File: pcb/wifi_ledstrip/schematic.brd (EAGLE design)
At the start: 80 x 49.5 mm, 64 parts, among them IC1 STM32F10XCXT6, Q1 8MHz

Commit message: gerber files exported
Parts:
- moved C1 0.61 mm to (69.4, 34.9)
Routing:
- net GND: track 350.7 -> 351.5 mm
- removed copper zone on layer 16, net SIGNATURE
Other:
- board text added: "v1.0"
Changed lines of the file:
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@@
 <text x="15.42" y="8.91" size="1.778" layer="21">+12V</text>
 <text x="42.672" y="9.144" size="1.778" layer="21">+12V</text>
-<text x="28.448" y="44.5008" size="1.778" layer="16" rot="MR0">Made by</text>
-<text x="28.448" y="41.2496" size="1.778" layer="16" rot="MR0">Daniel Tar</text>
-<text x="28.448" y="37.9984" size="1.778" layer="16" rot="MR0">30.07.2018</text>
+<text x="28.448" y="44.5008" size="1.778" layer="26" rot="MR0">Made by</text>
+<text x="28.448" y="41.2496" size="1.778" layer="26" rot="MR0">Daniel Tar</text>
+<text x="28.448" y="37.9984" size="1.778" layer="26" rot="MR0">30.07.2018</text>
+<text x="28.448" y="35.3568" size="1.778" layer="26" rot="MR0">v1.0</text>
 </plain>
 <attributes>
@@
 <attribute name="VALUE" x="66.17" y="38.81" size="1.27" layer="27" rot="R90"/>
 </element>
-<element name="C1" library="rcl" library_urn="urn:adsk.eagle:library:334" package="C1206" package3d_urn="urn:adsk.eagle:package:23618/2" value="" x="68.79" y="34.92" rot="R270">
-<attribute name="SPICEPREFIX" value="C" x="68.79" y="34.92" size="1.778" layer="27" rot="R270" display="off"/>
+<element name="C1" library="rcl" library_urn="urn:adsk.eagle:library:334" package="C1206" package3d_urn="urn:adsk.eagle:package:23618/2" value="" x="69.3996" y="34.92" rot="R270">
+<attribute name="SPICEPREFIX" value="C" x="69.3996" y="34.92" size="1.778" layer="27" rot="R270" display="off"/>
 </element>
 <element name="R7" library="rcl" library_urn="urn:adsk.eagle:library:334" package="R1206" package3d_urn="urn:adsk.eagle:package:23540/2" value="" x="23.42" y="47.29" rot="R180">
@@
 <wire x1="76.17" y1="21.17" x2="76.13" y2="21.21" width="0.2032" layer="1"/>
 <wire x1="77.75" y1="22.83" x2="76.13" y2="21.21" width="0.2032" layer="1"/>
-<wire x1="68.79" y1="33.52" x2="68.3775" y2="33.1075" width="0.508" layer="1"/>
-<wire x1="68.3775" y1="33.1075" x2="66.165" y2="33.1075" width="0.508" layer="1"/>
+<wire x1="69.3996" y1="33.52" x2="68.9871" y2="33.1075" width="0.508" layer="1"/>
+<wire x1="68.9871" y1="33.1075" x2="66.165" y2="33.1075" width="0.508" layer="1"/>
 <wire x1="76.16" y1="10.97" x2="76.16" y2="9.27" width="0.508" layer="1"/>
 <wire x1="76.16" y1="9.27" x2="73.25" y2="6.36" width="0.508" layer="1"/>
@@
 <wire x1="76.33" y1="46.17" x2="77.75" y2="44.75" width="0.508" layer="1"/>
 <wire x1="73.33" y1="46.17" x2="76.33" y2="46.17" width="0.508" layer="1"/>
-<wire x1="68.79" y1="33.52" x2="68.75" y2="33.48" width="0.5588" layer="1"/>
+<wire x1="69.3996" y1="33.52" x2="68.75" y2="32.8704" width="0.5588" layer="1"/>
 <via x="68.75" y="31.75" extent="1-16" drill="0.35"/>
 <wire x1="68.75" y1="31.75" x2="68.75" y2="23" width="0.5588" layer="16"/>
 <wire x1="65" y1="19.25" x2="64.75" y2="19.25" width="0.5588" layer="16"/>
 <via x="64.75" y="19.25" extent="1-16" drill="0.35"/>
-<wire x1="68.75" y1="33.48" x2="68.75" y2="31.75" width="0.5588" layer="1"/>
+<wire x1="68.75" y1="32.8704" x2="68.75" y2="31.75" width="0.5588" layer="1"/>
 <wire x1="68.75" y1="23" x2="65" y2="19.25" width="0.5588" layer="16"/>
 <polygon width="0.3048" layer="16" spacing="1.778" pour="hatch" isolate="0.2032" rank="2">
@@
 <vertex x="80.5" y="-0.25"/>
 <vertex x="80.5" y="50"/>
+</polygon>
+<polygon width="0.2032" layer="16" isolate="0.2032">
+<vertex x="14.4272" y="47.1424"/>
+<vertex x="14.4272" y="37.3888"/>
+<vertex x="29.2608" y="37.3888"/>
+<vertex x="29.2608" y="47.1424"/>
 </polygon>
 </signal>
@@
 <via x="66.75" y="38.5" extent="1-16" drill="0.35"/>
 <wire x1="66.75" y1="38.5" x2="67.25" y2="38.5" width="0.762" layer="1"/>
-<wire x1="67.25" y1="38.5" x2="68.79" y2="36.96" width="0.762" layer="1"/>
-<wire x1="68.79" y1="36.96" x2="68.79" y2="36.32" width="0.762" layer="1"/>
+<wire x1="67.25" y1="38.5" x2="69.3996" y2="36.3504" width="0.762" layer="1"/>
+<wire x1="69.3996" y1="36.3504" x2="69.3996" y2="36.32" width="0.762" layer="1"/>
 <wire x1="51.3" y1="32.95" x2="51.3" y2="36.45" width="0.2032" layer="1"/>
 <wire x1="51.3" y1="36.45" x2="50.25" y2="37.5" width="0.2032" layer="1"/>
@@
 <via x="65.01" y="46.08" extent="1-16" drill="3.1"/>
 </signal>
-<signal name="SIGNATURE">
-<polygon width="0.0254" layer="16" pour="cutout" isolate="0.2032">
-<vertex x="14.4272" y="47.1424"/>
-<vertex x="14.4272" y="37.3888"/>
-<vertex x="29.2608" y="37.3888"/>
-<vertex x="29.2608" y="47.1424"/>
-</polygon>
-</signal>
 </signals>
 <mfgpreviewcolors>
 <mfgpreviewcolor name="soldermaskcolor" color="0xC8008000"/>
-<mfgpreviewcolor name="silkscreencolor" color="0xFFFEFEFE"/>
+<mfgpreviewcolor name="silkscreencolor" color="0xFFFFFFFF"/>
 <mfgpreviewcolor name="backgroundcolor" color="0xFF282828"/>
 <mfgpreviewcolor name="coppercolor" color="0xFFFFBF00"/>

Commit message: electric parts arrived - pcb soldered
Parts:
- C1: value (none) -> 220u
- C2: value 0.1u -> 100n
- RFBT1: value 33.2 -> 33.2k
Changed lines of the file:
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@@
 <drawing>
 <settings>
-<setting alwaysvectorfont="yes"/>
+<setting alwaysvectorfont="no"/>
 <setting verticaltext="up"/>
 </settings>
@@
 <attribute name="VALUE" x="66.17" y="38.81" size="1.27" layer="27" rot="R90"/>
 </element>
-<element name="C1" library="rcl" library_urn="urn:adsk.eagle:library:334" package="C1206" package3d_urn="urn:adsk.eagle:package:23618/2" value="" x="69.3996" y="34.92" rot="R270">
+<element name="C1" library="rcl" library_urn="urn:adsk.eagle:library:334" package="C1206" package3d_urn="urn:adsk.eagle:package:23618/2" value="220u" x="69.3996" y="34.92" rot="R270">
 <attribute name="SPICEPREFIX" value="C" x="69.3996" y="34.92" size="1.778" layer="27" rot="R270" display="off"/>
 </element>
@@
 <attribute name="SPICEPREFIX" value="R" x="23.42" y="39.7" size="1.778" layer="27" rot="R180" display="off"/>
 </element>
-<element name="C2" library="rcl" library_urn="urn:adsk.eagle:library:334" package="C1206" package3d_urn="urn:adsk.eagle:package:23618/2" value="0.1u" x="16.2" y="28.75" smashed="yes" rot="R270">
+<element name="C2" library="rcl" library_urn="urn:adsk.eagle:library:334" package="C1206" package3d_urn="urn:adsk.eagle:package:23618/2" value="100n" x="16.2" y="28.75" smashed="yes" rot="R270">
 <attribute name="NAME" x="15.5968" y="33.0856" size="1.27" layer="25" rot="R270"/>
 <attribute name="SPICEPREFIX" value="C" x="16.2" y="28.75" size="1.778" layer="27" rot="R270" display="off"/>
@@
 <attribute name="VALUE" x="29.92" y="26.1" size="1.27" layer="27" rot="R90"/>
 </element>
-<element name="RFBT1" library="rcl" library_urn="urn:adsk.eagle:library:334" package="R1206" package3d_urn="urn:adsk.eagle:package:23540/2" value="33.2" x="25.21" y="27.37" smashed="yes" rot="R90">
+<element name="RFBT1" library="rcl" library_urn="urn:adsk.eagle:library:334" package="R1206" package3d_urn="urn:adsk.eagle:package:23540/2" value="33.2k" x="25.21" y="27.37" smashed="yes" rot="R90">
 <attribute name="NAME" x="24.102" y="24.732" size="1.27" layer="25" rot="R90"/>
 <attribute name="SPICEPREFIX" value="R" x="25.21" y="27.37" size="1.778" layer="27" rot="R90" display="off"/>

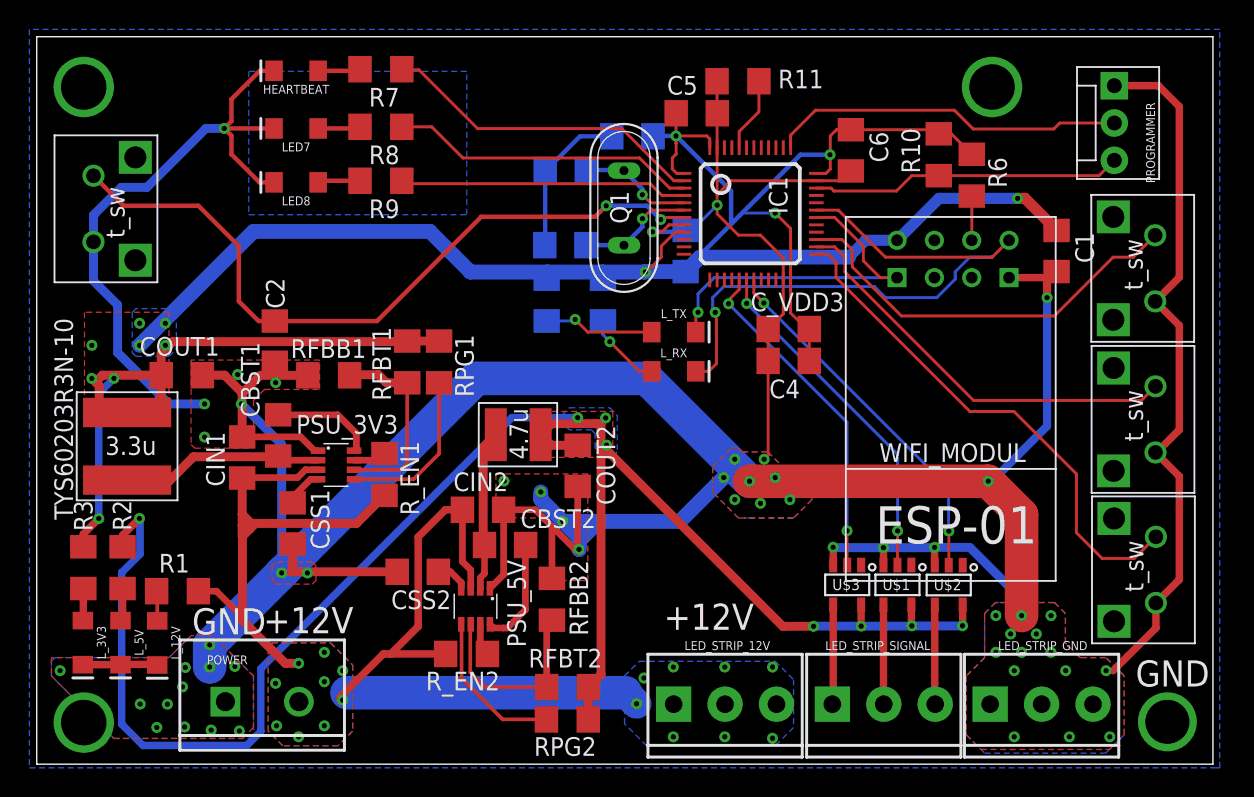
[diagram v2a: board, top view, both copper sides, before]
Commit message: pcb fix - boot1 pin pulled to gnd
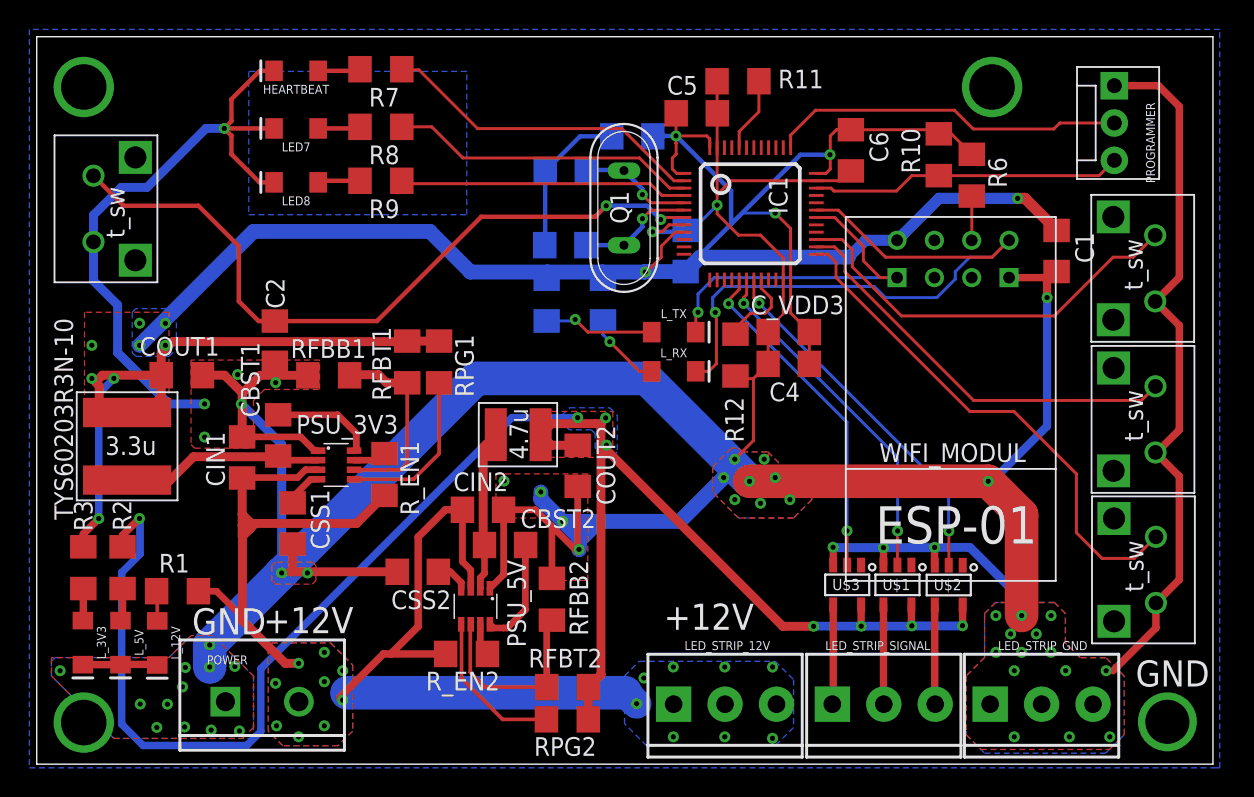
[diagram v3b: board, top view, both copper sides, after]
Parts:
- added R12: 10k, rcl:R1206
- moved C4 0.20 mm to (51.2, 27.2)
- moved C_VDD3 0.20 mm to (51.2, 29.4)
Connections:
- net N$16 renamed BOOT0
- new net BOOT1: IC1.20, R12.2
- net GND: now also R12.1
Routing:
- net BOOT1: track 0.00 -> 5.58 mm

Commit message: pcb fix - two more gnd polygon added
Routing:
- net GND: track 352.0 -> 354.5 mm
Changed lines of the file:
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@@
 <wire x1="47.5488" y1="26.4164" x2="47.7304" y2="26.2348" width="0.2032" layer="1"/>
 <wire x1="47.7304" y1="26.2348" x2="48.768" y2="26.2348" width="0.2032" layer="1"/>
+<wire x1="11.42" y1="24.51" x2="13.92" y2="24.51" width="0.6096" layer="16"/>
+<polygon width="0.2032" layer="16">
+<vertex x="12.3952" y="27.432"/>
+<vertex x="10.5664" y="25.6032"/>
+<vertex x="10.5664" y="24.7904"/>
+<vertex x="10.5664" y="22.1488"/>
+<vertex x="11.176" y="21.5392"/>
+<vertex x="12.5984" y="21.5392"/>
+<vertex x="14.8336" y="23.7744"/>
+<vertex x="14.8336" y="24.7904"/>
+<vertex x="15.4432" y="25.4"/>
+<vertex x="16.8656" y="25.4"/>
+<vertex x="17.272" y="25.8064"/>
+<vertex x="17.272" y="26.416"/>
+<vertex x="17.272" y="27.0256"/>
+<vertex x="16.8656" y="27.432"/>
+</polygon>
+<polygon width="0.2032" layer="16">
+<vertex x="31.496" y="19.9136"/>
+<vertex x="34.9504" y="19.9136"/>
+<vertex x="37.592" y="17.272"/>
+<vertex x="37.592" y="16.8656"/>
+<vertex x="37.592" y="14.0208"/>
+<vertex x="37.1856" y="13.6144"/>
+<vertex x="35.7632" y="13.6144"/>
+<vertex x="35.3568" y="14.0208"/>
+<vertex x="35.3568" y="15.6464"/>
+<vertex x="35.56" y="15.8496"/>
+<vertex x="32.9184" y="18.4912"/>
+<vertex x="31.496" y="18.4912"/>
+<vertex x="31.2928" y="18.6944"/>
+<vertex x="31.2928" y="19.7104"/>
+</polygon>
 </signal>
 <signal name="LED_STRIP_SIGNAL_1">

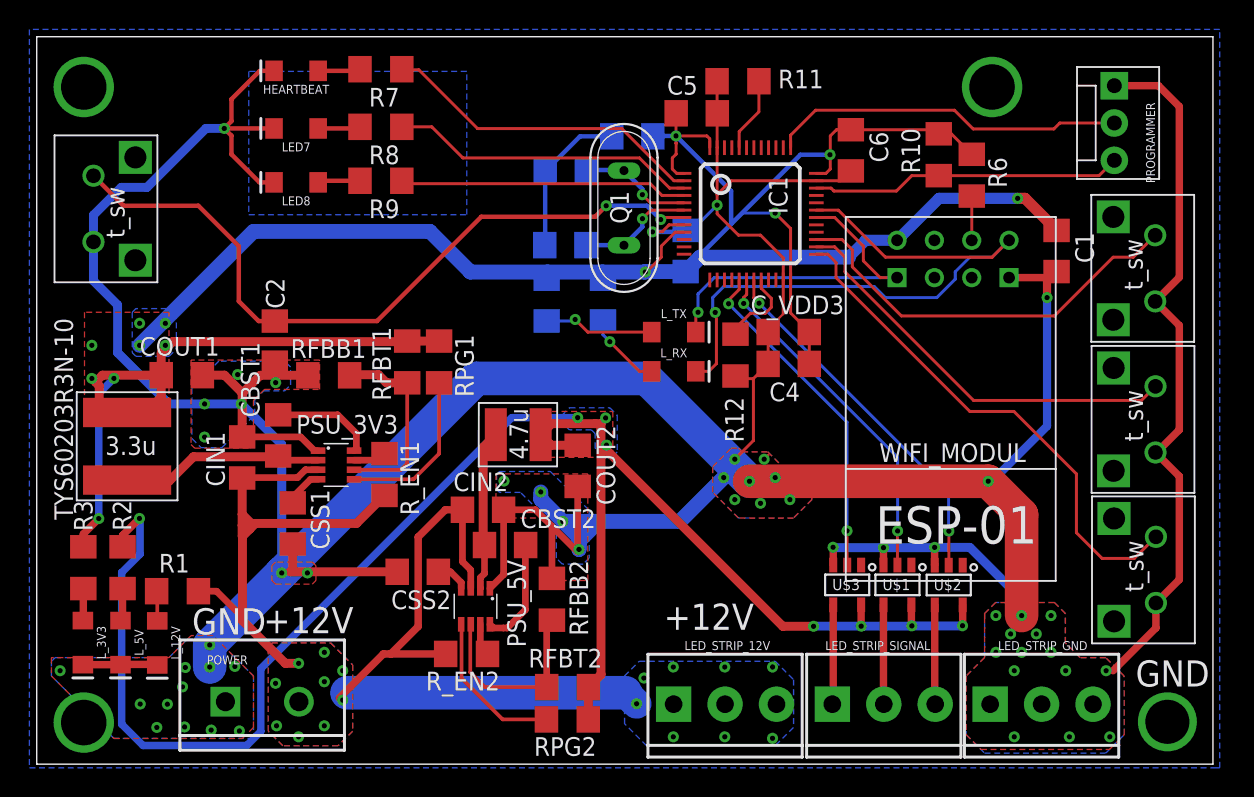
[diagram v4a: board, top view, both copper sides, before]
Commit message: pcb fixed - 2 wires were mixed up - bigger capacitance to SS pin
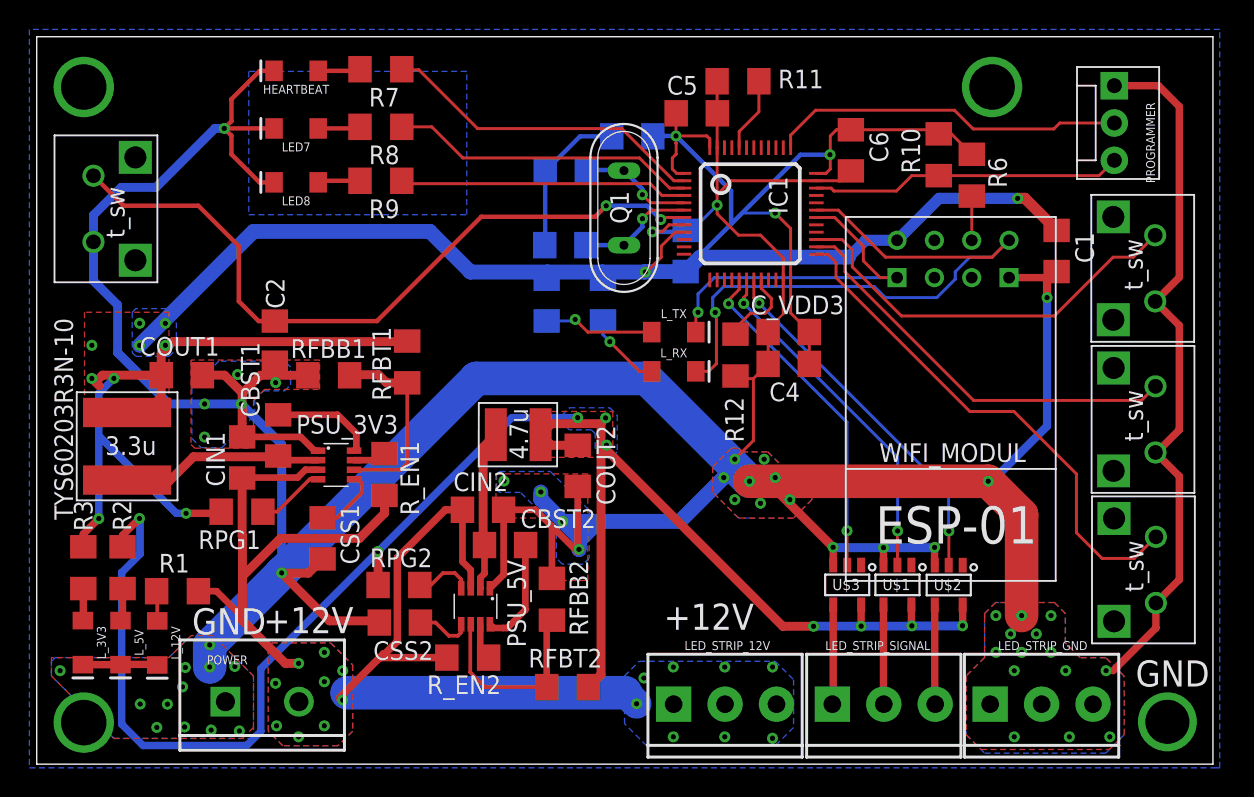
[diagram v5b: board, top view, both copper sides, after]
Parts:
- CSS1, CSS2: value 8.2n -> 100n
- moved RPG1 16.8 mm to (14.0, 17.2), turned to 180 degrees
- moved RPG2 14.7 mm to (24.6, 12.2), turned to 180 degrees
- moved CSS2 3.66 mm to (24.7, 9.64)
- moved CSS1 2.27 mm to (19.5, 15.4)
- moved R_EN2 0.26 mm to (29.3, 7.25)
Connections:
- removed net N$25: CSS1.1, PSU_3V3.4
- removed net N$28: PSU_3V3.5, RPG1.1
- removed net N$30: CSS2.1, PSU_5V.4
- removed net N$34: PSU_5V.5, RPG2.1
- new net N$PG1: PSU_3V3.4, RPG1.1
- new net N$PG2: PSU_5V.4, RPG2.1
- new net N$SS1: CSS1.1, PSU_3V3.5
- new net N$SS2: CSS2.1, PSU_5V.5
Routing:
- net N$28: track 11.3 -> 0.00 mm
- net N$34: track 10.6 -> 0.00 mm
- net +3V3: track 180.0 -> 186.9 mm, vias 13 -> 14
- net N$SS1: track 0.00 -> 4.69 mm
- net N$PG1: track 0.00 -> 4.67 mm
- net N$PG2: track 0.00 -> 3.93 mm
- net N$SS2: track 0.00 -> 3.79 mm
- net N$25: track 2.62 -> 0.00 mm
- net N$30: track 2.26 -> 0.00 mm
- net GND: track 354.5 -> 355.8 mm, vias 53 -> 52
- net +12V: track 83.3 -> 84.2 mm
- net +5V: track 122.1 -> 122.2 mm, vias 8 -> 9
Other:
- board text added: "14.10.2018"
- board text added: "v1.1"
- board text removed: "30.07.2018"
- board text removed: "v1.0"
